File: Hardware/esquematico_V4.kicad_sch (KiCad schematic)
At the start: 46 parts, among them J1 Conn_SPI, J11 Conn_01x02_Socket, J12 Conn_SPI, J14 Conn_01x02_Socket, J15 Conn_01x02_Socket, J16 Conn_01x02_Socket, J17 Conn_01x02_Socket, J18 Conn_01x02_Socket, J19 Conn_01x02_Socket, J2 Conn_DHT, J20 Conn_01x02_Socket, J21 Conn_01x02_Socket, J22 Conn_01x02_Socket, J23 RJ45, J24 RJ45, J25 RJ45, J3 Conn_SPI, J4 Conn_cartao_SD, J5 Conn_BH1750, J6 Conn_BMP, J7 Conn_Lora_4, J8 Conn_02x06_Row_Letter_Last, U1 DHT22, U2 module_bh1750, U3 module_bme280, U4 Lora_Sx1276, U6 MicroSD Card Adapter, U7 NUCLEO-F446RE

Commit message: hardware: inicia PCB V2
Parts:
- removed C1, C2, C3: 100n, Capacitor_THT:C_Disc_D3.8mm_W2.6mm_P2.50mm, symbol Device:C
- removed J17, J18, J19, J20, J21, J22: Conn_01x02_Socket, Connector_PinSocket_2.54mm:PinSocket_1x02_P2.54mm_Vertical, symbol Connector:Conn_01x02_Socket
- removed R1: 500, Resistor_THT:R_Axial_DIN0204_L3.6mm_D1.6mm_P7.62mm_Horizontal, symbol Device:R
- removed R2: 2000, Resistor_THT:R_Axial_DIN0204_L3.6mm_D1.6mm_P7.62mm_Horizontal, symbol Device:R
- removed R3: 5k, Resistor_THT:R_Axial_DIN0204_L3.6mm_D1.6mm_P7.62mm_Horizontal, symbol Device:R
- removed R4, R9: 10k, Resistor_THT:R_Axial_DIN0204_L3.6mm_D1.6mm_P7.62mm_Horizontal, symbol Device:R
- removed R5, R6: 1k, Resistor_THT:R_Axial_DIN0204_L3.6mm_D1.6mm_P7.62mm_Horizontal, symbol Device:R
- removed S1, S2, S3, S4, S5, S6: MISM7R1015, myLibrary:Reed_Switch, symbol Reed_Switch:MISM7R1015
- added C4, C5: 100n, Capacitor_THT:C_Disc_D3.8mm_W2.6mm_P2.50mm, symbol Device:C
- added R10, R11: 10k, Resistor_THT:R_Axial_DIN0204_L3.6mm_D1.6mm_P7.62mm_Horizontal, symbol Device:R
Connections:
- net +3V3: now also J15.1 (Pin_1); no longer J14.1 (Pin_1), J14.2 (Pin_2), J16.2 (Pin_2)
- net CN10_GND: now also J14.2 (Pin_2), C4.2, C5.2, R10.1, R11.1; no longer J15.1 (Pin_1), J15.2 (Pin_2)
- net PA0: now also J14.1 (Pin_1), R8.1
- net PA1: now also J16.2 (Pin_2), C4.1, R10.2
- net PC7: now also J15.2 (Pin_2), C5.1, R11.2; no longer R8.1
- net PB0: no longer names the net of U7.CN7_34 (PB0)
- no-connect marks 7 -> 72

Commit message: hardware: adiciona sensores e cartao SD
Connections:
- net PB6: no longer U7.CN10_17 (PB6)
- net PB7: no longer U7.CN7_21 (PB7)
- new net SCK: U7.CN10_17 (PB6)
- new net SDA: U7.CN7_21 (PB7)
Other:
- added sheet BH1750 (bh1750.kicad_sch)
- added sheet BMP280 (untitled.kicad_sch)
- added sheet Cartao SD (cartao_sd.kicad_sch)
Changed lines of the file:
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@@
 		)
 	)
-	(global_label "PB7"
+	(global_label "SDA"
 		(shape input)
 		(at 194.31 -36.83 180)
@@
 		)
 		(property "Intersheetrefs" "${INTERSHEET_REFS}"
-			(at 187.5753 -36.83 0)
+			(at 187.7567 -36.83 0)
 			(effects
 				(font
@@
 		)
 	)
-	(global_label "PB6"
+	(global_label "SCK"
 		(shape input)
 		(at 256.54 -31.75 180)
@@
 	)
 	(sheet
+		(at 33.02 93.98)
+		(size 38.1 20.32)
+		(exclude_from_sim no)
+		(in_bom yes)
+		(on_board yes)
+		(dnp no)
+		(fields_autoplaced yes)
+		(stroke
+			(width 0.1524)
+			(type solid)
+		)
+		(fill
+			(color 0 0 0 0.0000)
+		)
+		(property "Sheetname" "BMP280"
+			(at 33.02 93.2684 0)
+			(effects
+				(font
+					(size 1.27 1.27)
+				)
+				(justify left bottom)
+			)
+		)
+		(property "Sheetfile" "untitled.kicad_sch"
+			(at 33.02 114.8846 0)
+			(effects
+				(font
+					(size 1.27 1.27)
+				)
+				(justify left top)
+			)
+		)
+		(instances
+			(project "esquematico_V4"
+				(path "/0c305a6e-f9cd-49a1-b146-c2956e5469b6"
+					(page "4")
+				)
+			)
+		)
+	)
+	(sheet
 		(at 30.48 134.62)
 		(size 25.4 16.51)
@@
 	)
 	(sheet
+		(at 80.01 134.62)
+		(size 29.21 15.24)
+		(exclude_from_sim no)
+		(in_bom yes)
+		(on_board yes)
+		(dnp no)
+		(fields_autoplaced yes)
+		(stroke
+			(width 0.1524)
+			(type solid)
+		)
+		(fill
+			(color 0 0 0 0.0000)
+		)
+		(property "Sheetname" "Cartao SD"
+			(at 80.01 133.9084 0)
+			(effects
+				(font
+					(size 1.27 1.27)
+				)
+				(justify left bottom)
+			)
+		)
+		(property "Sheetfile" "cartao_sd.kicad_sch"
+			(at 80.01 150.4446 0)
+			(effects
+				(font
+					(size 1.27 1.27)
+				)
+				(justify left top)
+			)
+		)
+		(instances
+			(project "esquematico_V4"
+				(path "/0c305a6e-f9cd-49a1-b146-c2956e5469b6"
+					(page "6")
+				)
+			)
+		)
+	)
+	(sheet
 		(at 93.98 25.4)
 		(size 39.37 16.51)
@@
 				)
 			)
+		)
+	)
+	(sheet
+		(at 91.44 93.98)
+		(size 29.21 16.51)
+		(exclude_from_sim no)
+		(in_bom yes)
+		(on_board yes)
+		(dnp no)
+		(fields_autoplaced yes)
+		(stroke
+			(width 0.1524)
+			(type solid)
+		)
+		(fill
+			(color 0 0 0 0.0000)
+		)
+		(property "Sheetname" "BH1750"
+			(at 91.44 93.2684 0)
+			(effects
+				(font
+					(size 1.27 1.27)
+				)
+				(justify left bottom)
+			)
+		)
+		(property "Sheetfile" "bh1750.kicad_sch"
+			(at 91.44 111.0746 0)
+			(effects
+				(font
+					(size 1.27 1.27)
+				)
+				(justify left top)
+			)
+		)
+		(instances
+			(project "esquematico_V4"
+				(path "/0c305a6e-f9cd-49a1-b146-c2956e5469b6"
+					(page "5")
+				)
+			)

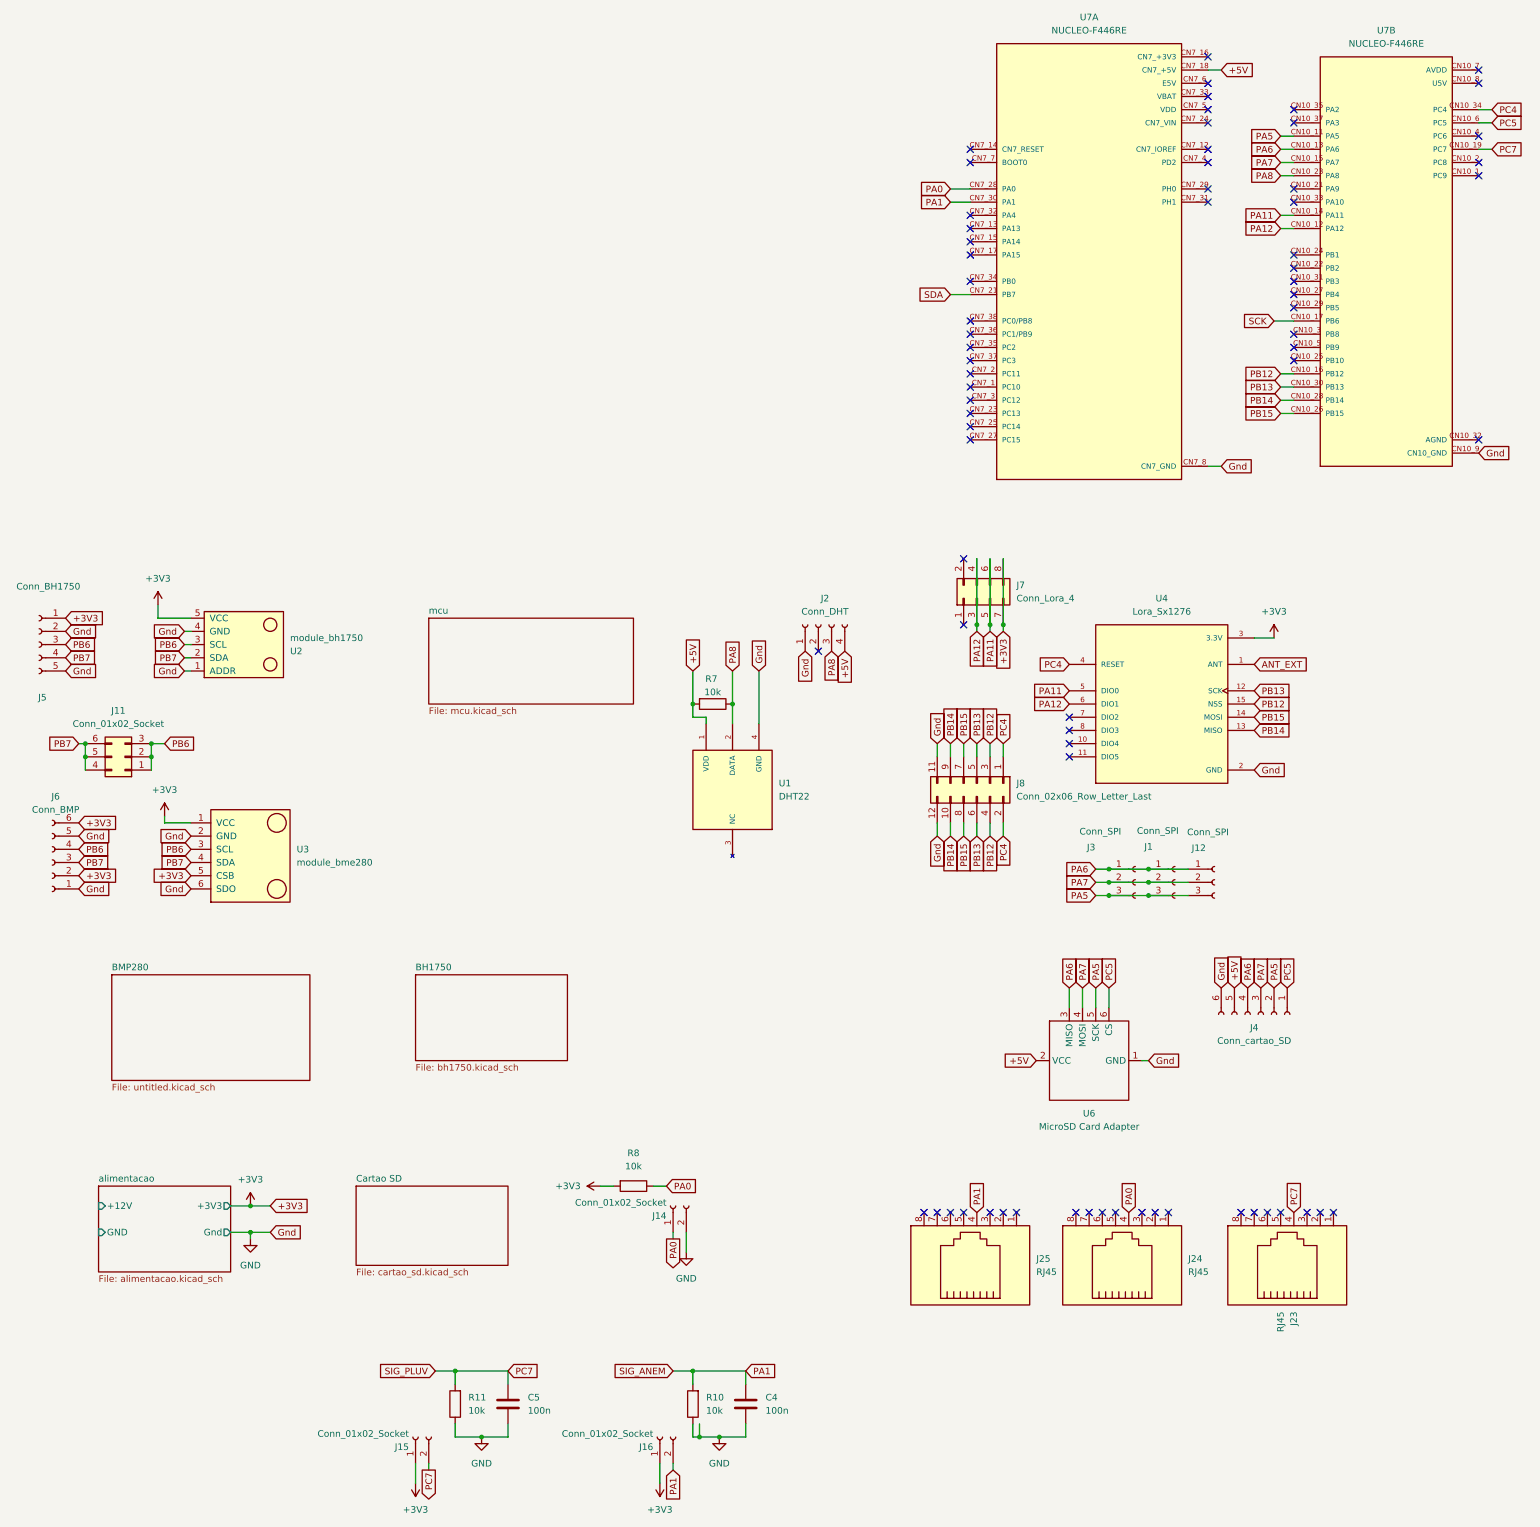
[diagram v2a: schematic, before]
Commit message: Add subfolhas DHT22 e LORA
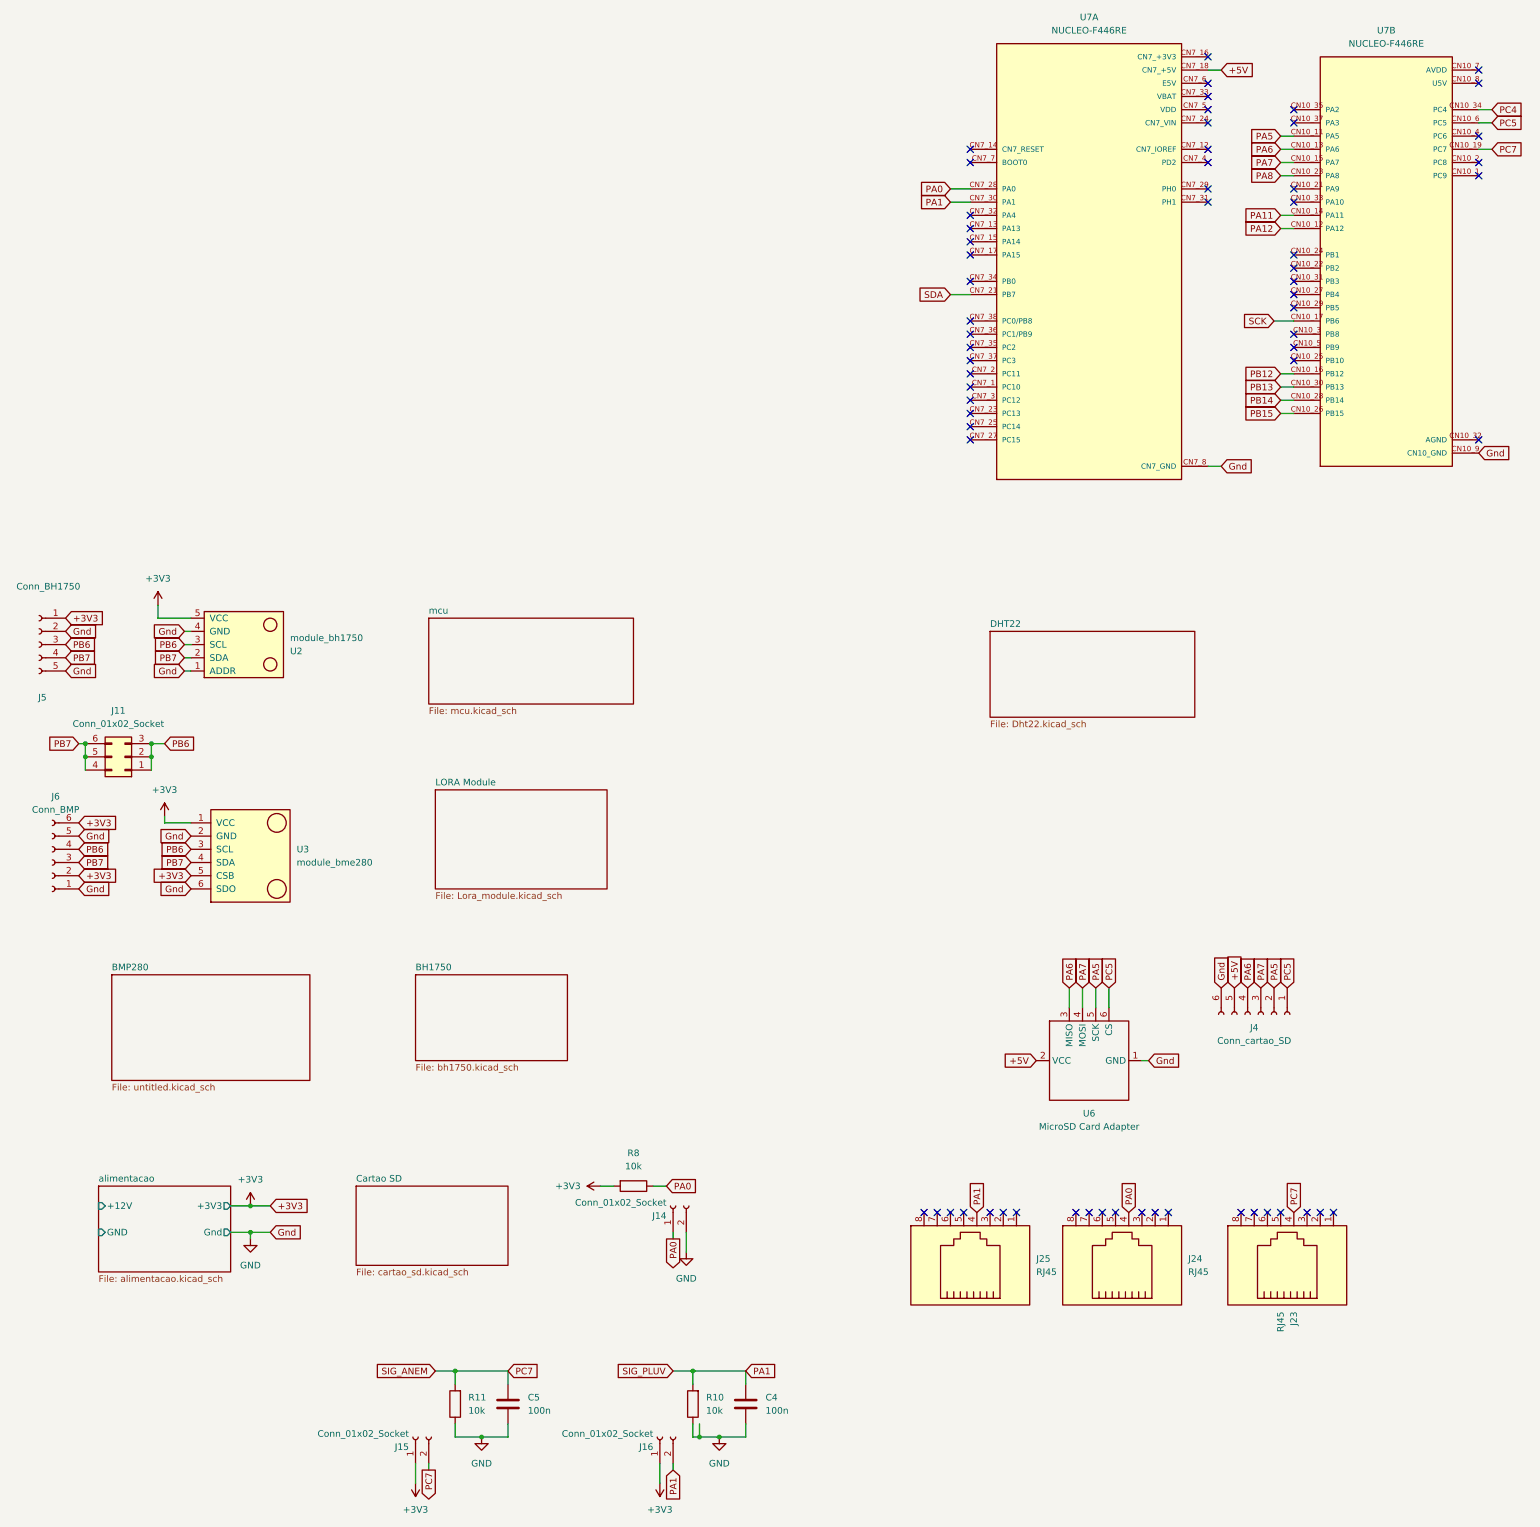
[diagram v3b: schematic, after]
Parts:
- removed J1, J12, J3: Conn_SPI, Connector_PinSocket_2.54mm:PinSocket_1x03_P2.54mm_Vertical, symbol Connector:Conn_01x03_Socket
- removed J2: Conn_DHT, Connector_PinSocket_2.54mm:PinSocket_1x04_P2.54mm_Vertical, symbol Connector:Conn_01x04_Socket
- removed J7: Conn_Lora_4, Connector_PinSocket_2.54mm:PinSocket_2x04_P2.54mm_Vertical, symbol Connector_Generic:Conn_02x04_Odd_Even
- removed J8: Conn_02x06_Row_Letter_Last, Connector_PinSocket_2.54mm:PinSocket_2x06_P2.54mm_Vertical, symbol Connector_Generic:Conn_02x06_Odd_Even
- removed R7: 10k, Resistor_THT:R_Axial_DIN0204_L3.6mm_D1.6mm_P7.62mm_Horizontal, symbol Device:R
- removed U1: DHT22, myLibrary:XDCR_DHT22, symbol DHT22_modulo:DHT22
- removed U4: Lora_Sx1276, myLibrary:SX1276_modulo, symbol SX1276_modulo:RA-01H
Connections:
- no-connect marks 72 -> 65
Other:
- added sheet DHT22 (Dht22.kicad_sch)
- added sheet LORA Module (Lora_module.kicad_sch)

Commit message: add sensores metereológicos - ajuda GPT
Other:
- added sheet METEOROLOGIA (Sensores_meteorologicos/meteorologia.kicad_sch)
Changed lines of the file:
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@@
 	(wire
 		(pts
+			(xy 182.88 80.01) (xy 198.12 80.01)
+		)
+		(stroke
+			(width 0)
+			(type default)
+		)
+	)
+	(wire
+		(pts
 			(xy 104.14 182.88) (xy 109.22 182.88)
 		)
@@
 	(wire
 		(pts
+			(xy 182.88 87.63) (xy 198.12 87.63)
+		)
+		(stroke
+			(width 0)
+			(type default)
+		)
+	)
+	(wire
+		(pts
+			(xy 182.88 72.39) (xy 198.12 72.39)
+		)
+		(stroke
+			(width 0)
+			(type default)
+		)
+	)
+	(wire
+		(pts
 			(xy 140.97 187.96) (xy 140.97 189.23)
 		)
@@
 		)
 	)
+	(global_label "RAIN_PULSE"
+		(shape input)
+		(at 198.12 72.39 0)
+		(effects
+			(font
+				(size 1.27 1.27)
+			)
+			(justify left)
+		)
+		(property "Intersheetrefs" "${INTERSHEET_REFS}"
+			(at 198.12 72.39 0)
+			(effects
+				(font
+					(size 1.27 1.27)
+				)
+				(hide yes)
+			)
+		)
+	)
 	(global_label "PB7"
 		(shape input)
@@
 		)
 	)
+	(global_label "WIND_SPEED_PULSE"
+		(shape input)
+		(at 198.12 80.01 0)
+		(effects
+			(font
+				(size 1.27 1.27)
+			)
+			(justify left)
+		)
+		(property "Intersheetrefs" "${INTERSHEET_REFS}"
+			(at 198.12 80.01 0)
+			(effects
+				(font
+					(size 1.27 1.27)
+				)
+				(hide yes)
+			)
+		)
+	)
 	(global_label "+3V3"
 		(shape input)
@@
 		)
 	)
+	(global_label "WIND_DIR_ADC"
+		(shape input)
+		(at 198.12 87.63 0)
+		(effects
+			(font
+				(size 1.27 1.27)
+			)
+			(justify left)
+		)
+		(property "Intersheetrefs" "${INTERSHEET_REFS}"
+			(at 198.12 87.63 0)
+			(effects
+				(font
+					(size 1.27 1.27)
+				)
+				(hide yes)
+			)
+		)
+	)
 	(symbol
 		(lib_id "Connector:RJ45")
@@
 				)
 			)
+		)
+	)
+	(sheet
+		(at 139.7 64.77)
+		(size 43.18 33.02)
+		(exclude_from_sim no)
+		(in_bom yes)
+		(on_board yes)
+		(dnp no)
+		(fields_autoplaced yes)
+		(stroke
+			(width 0.1524)
+			(type solid)
+		)
+		(fill
+			(color 0 0 0 0.0000)
+		)
+		(property "Sheetname" "METEOROLOGIA"
+			(at 139.7 64.0584 0)
+			(effects
+				(font
+					(size 1.27 1.27)
+				)
+				(justify left bottom)
+			)
+		)
+		(property "Sheetfile" "Sensores_meteorologicos/meteorologia.kicad_sch"
+			(at 139.7 98.5522 0)
+			(effects
+				(font
+					(size 1.27 1.27)
+				)
+				(justify left top)
+			)
+		)
+		(pin "RAIN_PULSE" output
+			(at 182.88 72.39 0)
+			(effects
+				(font
+					(size 1.27 1.27)
+				)
+				(justify right)
+			)
+		)
+		(pin "WIND_SPEED_PULSE" output
+			(at 182.88 80.01 0)
+			(effects
+				(font
+					(size 1.27 1.27)
+				)
+				(justify right)
+			)
+		)
+		(pin "WIND_DIR_ADC" output
+			(at 182.88 87.63 0)
+			(effects
+				(font
+					(size 1.27 1.27)
+				)
+				(justify right)
+			)
+		)
+		(instances
+			(project "esquematico_V4"
+				(path "/0c305a6e-f9cd-49a1-b146-c2956e5469b6"
+					(page "9")
+				)
+			)

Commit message: Sensores metereologicos -IA que fez
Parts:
- removed C4, C5: 100n, Capacitor_THT:C_Disc_D3.8mm_W2.6mm_P2.50mm, symbol Device:C
- removed J14, J15, J16: Conn_01x02_Socket, Connector_PinSocket_2.54mm:PinSocket_1x02_P2.54mm_Vertical, symbol Connector:Conn_01x02_Socket
- removed J23, J24, J25: RJ45, Connector_RJ:RJ45_RCH_RC01937, symbol Connector:RJ45
- removed R10, R11, R8: 10k, Resistor_THT:R_Axial_DIN0204_L3.6mm_D1.6mm_P7.62mm_Horizontal, symbol Device:R
- removed U7: NUCLEO-F446RE, myLibrary:MODULE_NUCLEO-F446RE, symbol Nucleo_F446:NUCLEO-F446RE
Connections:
- net CN10_GND renamed GND
- no-connect marks 65 -> 0
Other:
- sheet METEOROLOGIA: file Sensores_meteorologicos/meteorologia.kicad_sch -> meteorologia.kicad_sch
- sheet METEOROLOGIA ports: added VREF_SENSOR; removed none
- sheet alimentacao ports: added none; removed Gnd
- sheet mcu ports: added RAIN_PULSE, VREF_SENSOR, WIND_DIR_ADC, WIND_SPEED_PULSE; removed none

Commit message: design sensores pronto
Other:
- sheet LORA Module ports: added Lora_DIO0, Lora_DIO1, Lora_DIO2, Lora_MISO, Lora_MOSI, Lora_NSS, Lora_RST, Lora_SCK; removed none

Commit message: hardware: implementa alimentacao e adiciona bibliotecas locais - ajuda gpt
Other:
- sheet alimentacao ports: added +5V; removed +12V
